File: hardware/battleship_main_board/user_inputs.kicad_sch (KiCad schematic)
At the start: 5 parts

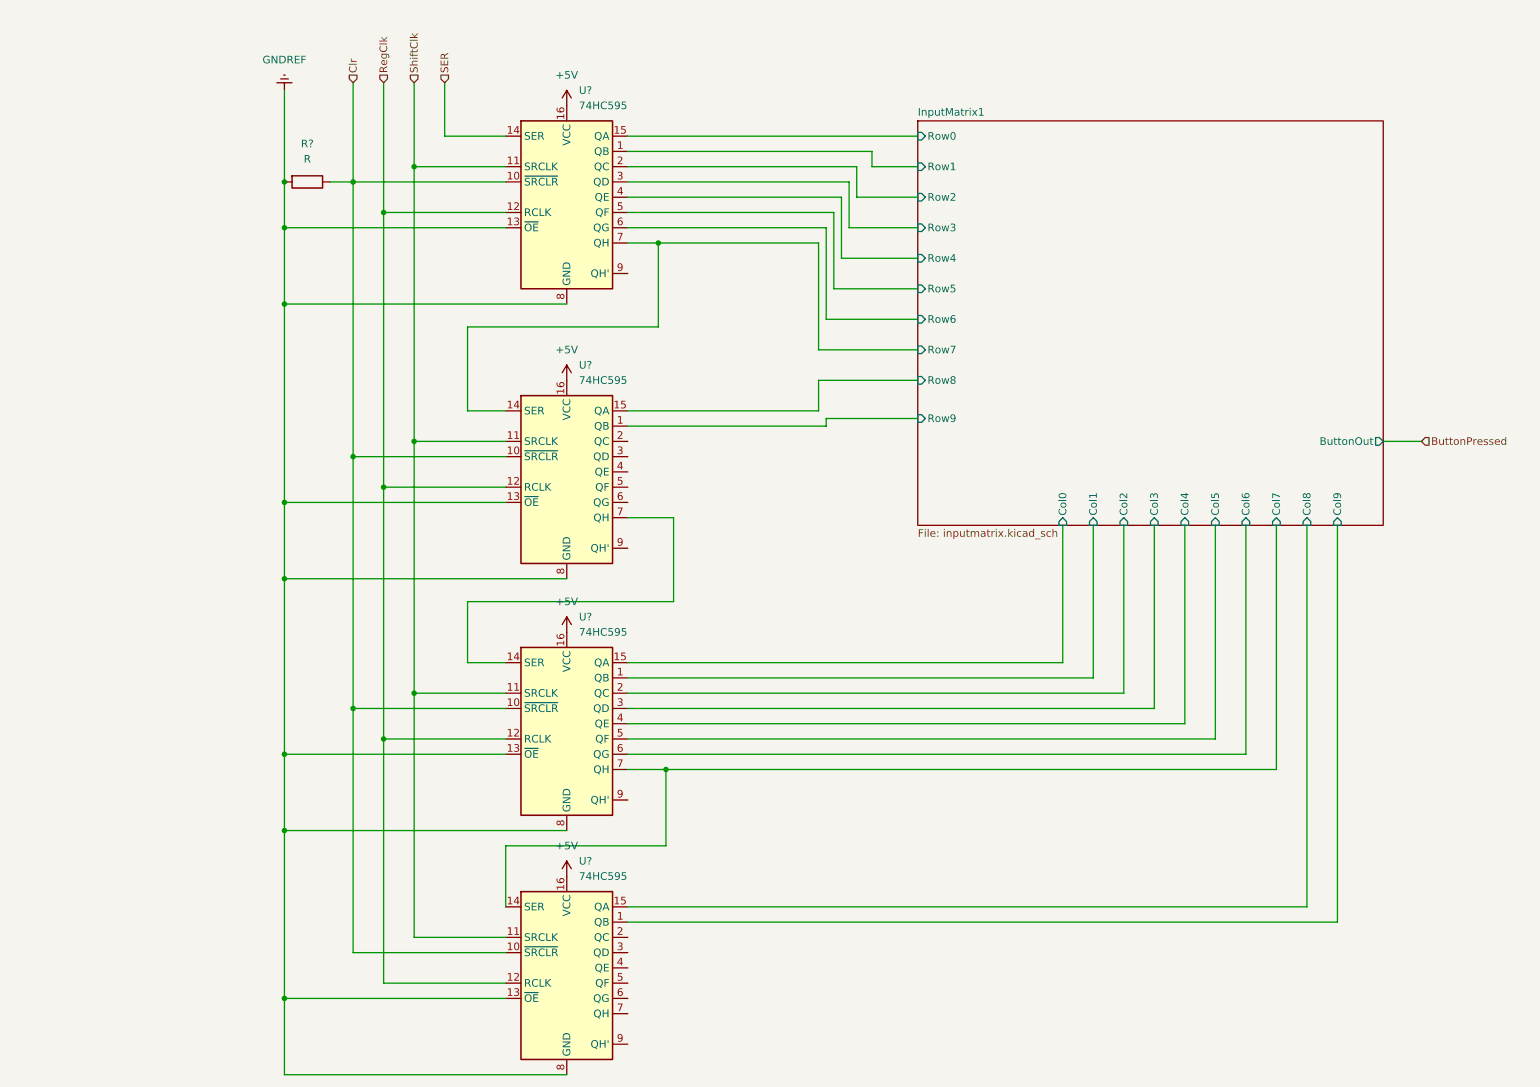
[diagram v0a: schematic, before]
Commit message: Got schematic to place that can be turned into a ratsnest
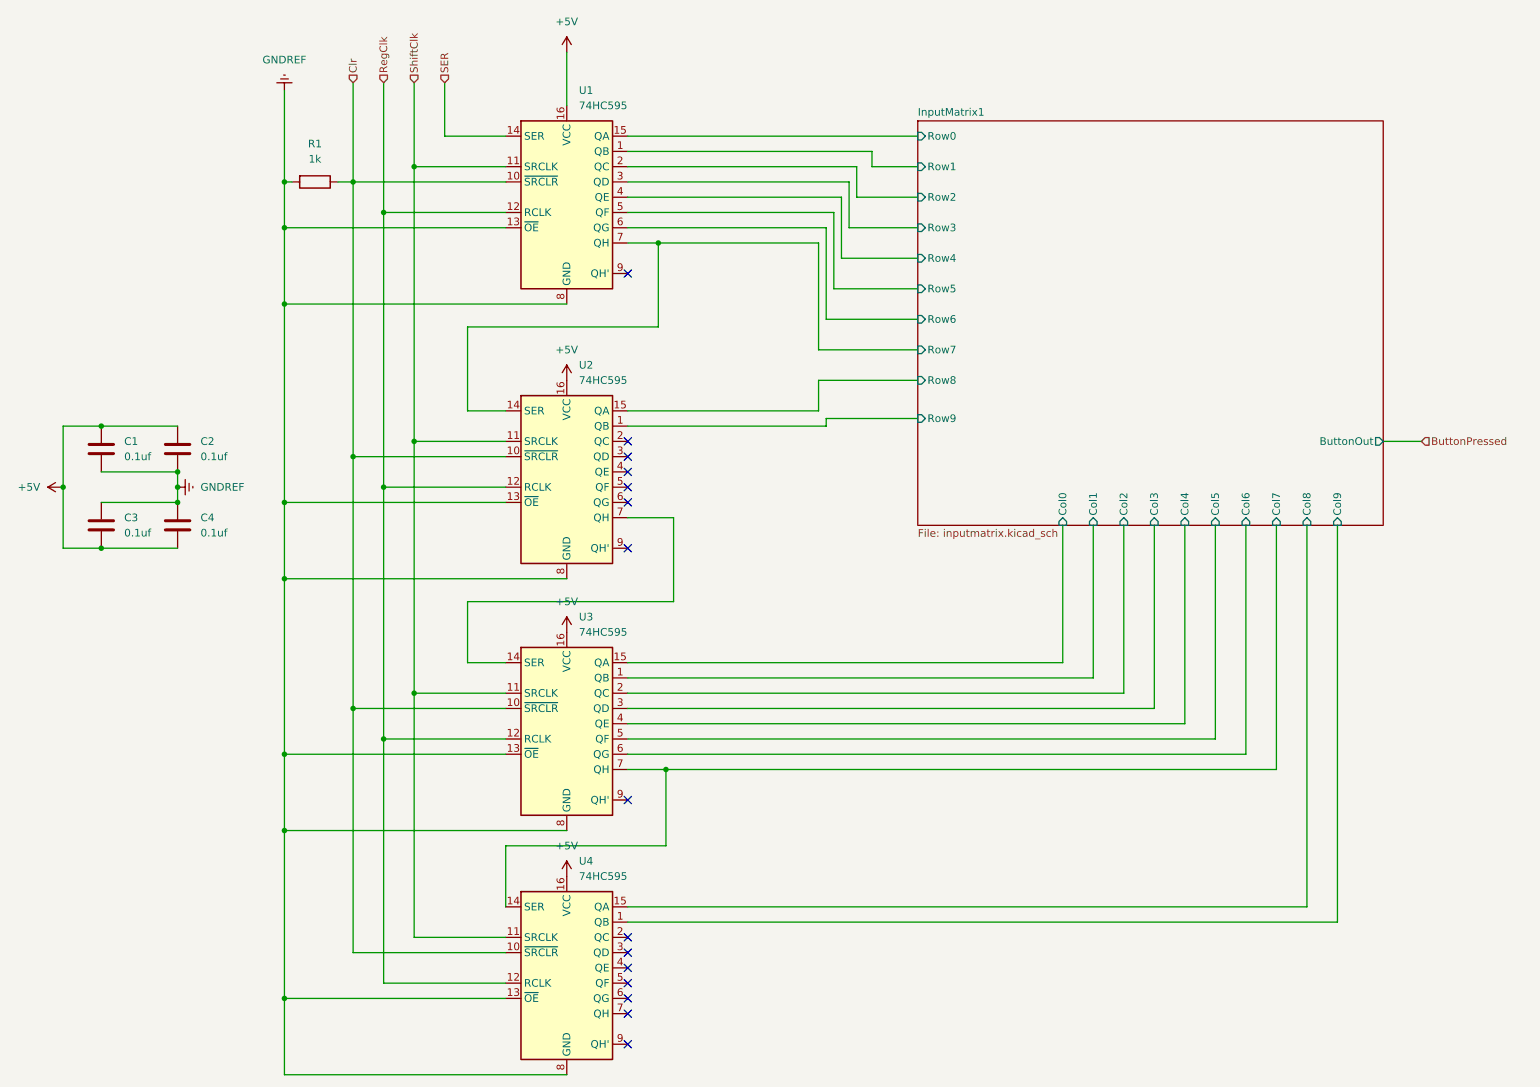
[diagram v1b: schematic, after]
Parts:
- added C1, C2, C3, C4: 0.1uf, Capacitor_THT:C_Disc_D3.0mm_W1.6mm_P2.50mm, symbol Device:C
- R1: renamed from R?; value R -> 1k; footprint (none) -> Resistor_THT:R_Axial_DIN0207_L6.3mm_D2.5mm_P10.16mm_Horizontal
- U1, U2, U3, U4: renamed from U?; footprint (none) -> Package_DIP:DIP-16_W7.62mm
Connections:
- net +5V: now also C1.1, C2.1, C3.2, C4.2
- net GNDREF: now also C1.2, C2.2, C3.1, C4.1
- no-connect marks 0 -> 15
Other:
- moved on the sheet: R1
